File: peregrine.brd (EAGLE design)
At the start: 55.9 x 55.9 mm, 70 parts, among them IC2 LMV358IDGKR, J1 USB MICRO, U1 ITG-3200, U2 ADXL345, U4 3.3V, U5 ATMEGA32U4-XUAU, Y1 16MHz KX-7

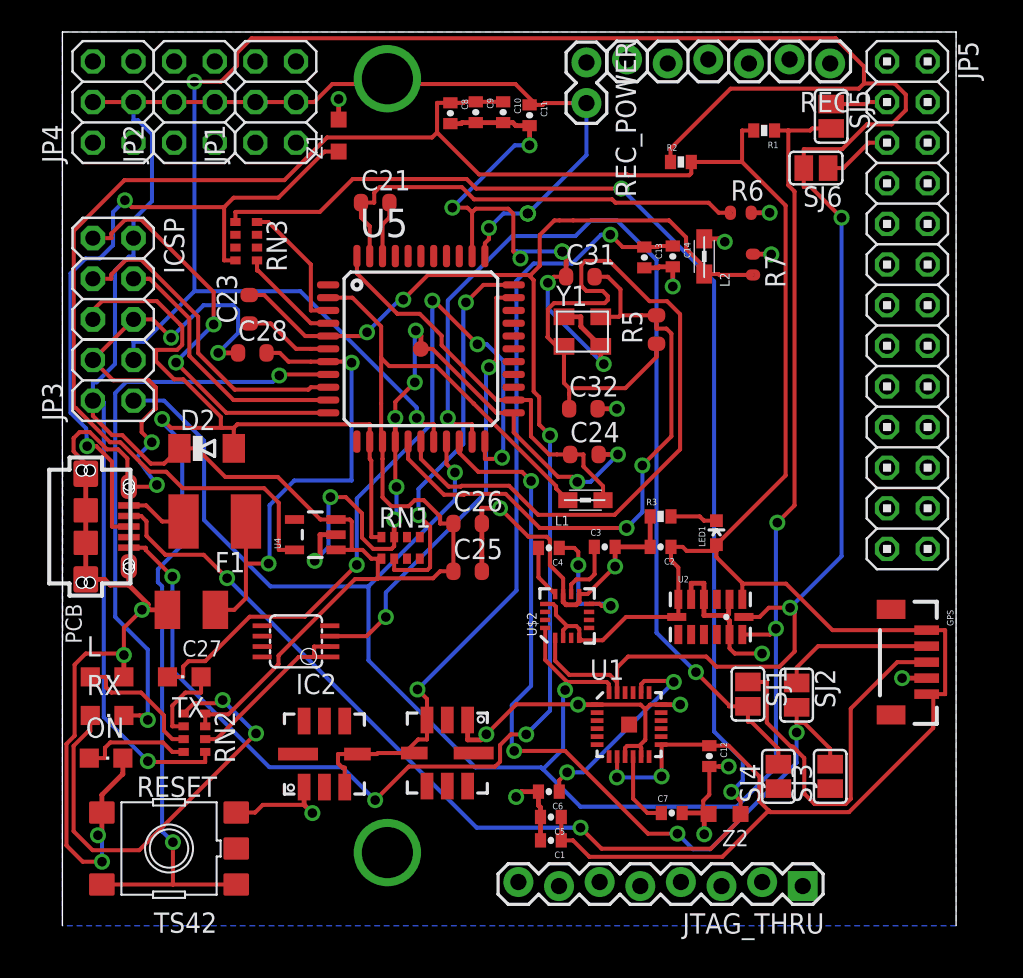
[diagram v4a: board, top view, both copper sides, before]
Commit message: Many changes.
Added level conversion to schematic. Had to re-do route because of many
added components. Also, connected a number of things which needed
connections in schematic. Route about 80% done.
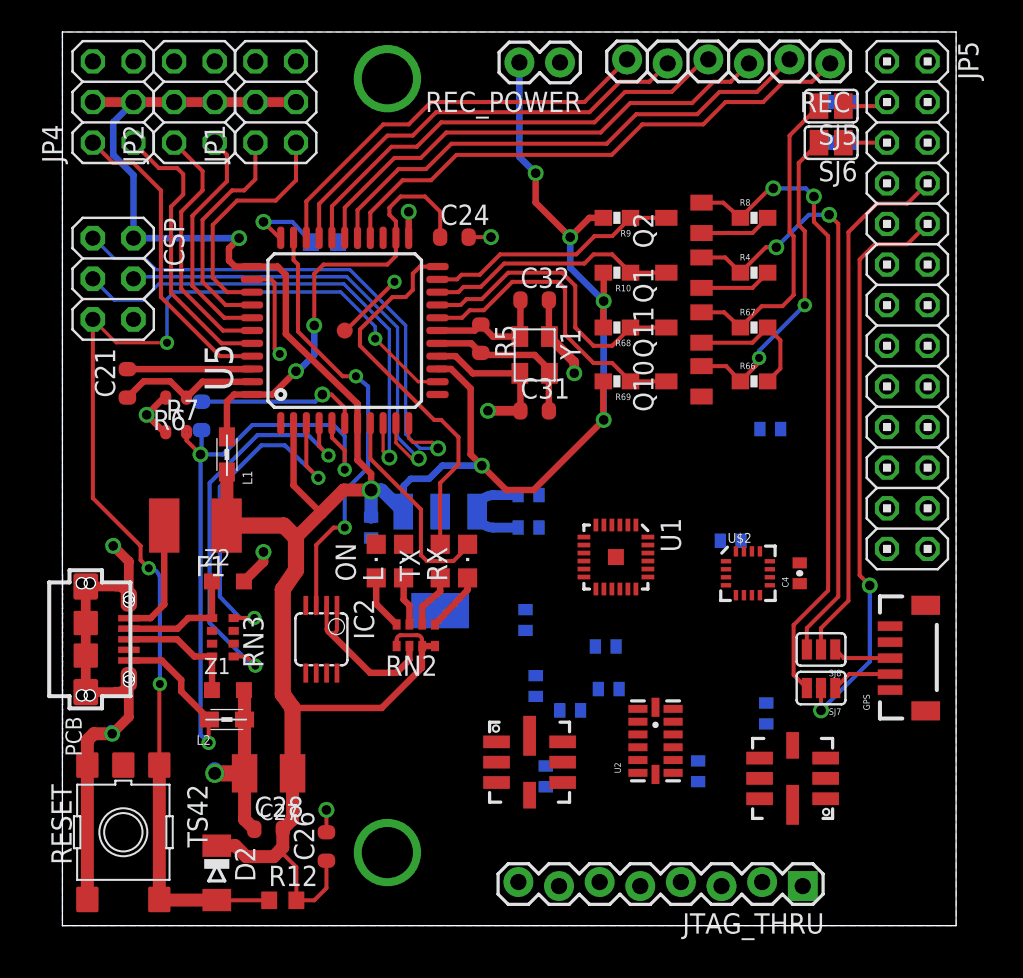
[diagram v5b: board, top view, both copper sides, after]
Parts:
- removed C25: 100n, SmartPrj:C0603-ROUND
- removed JP3: (no value), pinhead:2X02
- removed LED1: Blue, SparkFun:LED-0603
- removed R3: 330, SparkFun:0402-RES
- removed RN1: 10K, resistor-dil:CAY16
- removed SJ1, SJ2, SJ3, SJ4: (no value), jumper:SJ
- removed U4: 3.3V, SparkFun:SOT23-5
- added IC1: (no value), linear-technology:SOT223
- added Q1, Q10, Q11, Q2: BSS123, transistor-small-signal:SOT23
- added R10, R4, R66, R67, R68, R69, R8, R9: 10k, SparkFun:0603-RES
- added R11, R12: 10k, resistor:R0603
- added SJ7, SJ8: (no value), SparkFun:SJ_3
- moved L2 41.6 mm to (10.3, 12.9), turned to 0 degrees
- moved R7 37.6 mm to (7.11, 30.9), turned to 0 degrees
- moved R6 37.1 mm to (7.11, 33.0), turned to 180 degrees
- moved C8 36.2 mm to (29.6, 15.0), flipped to the bottom
- moved Z1 35.4 mm to (10.4, 14.7), turned to 0 degrees
- moved Z2 34.3 mm to (10.4, 21.5), turned to 0 degrees
- moved C14 33.5 mm to (30.2, 9.33), flipped to the bottom
- moved C13 32.3 mm to (39.8, 9.65), flipped to the bottom
- moved C9 31.9 mm to (29.0, 19.1), flipped to the bottom
- moved C28 29.8 mm to (12.9, 6.03)
- moved U$4 29.3 mm to (45.7, 9.21), turned to 180 degrees
- moved C11 27.6 mm to (19.3, 24.9), flipped to the bottom
- moved D2 26.6 mm to (9.65, 3.30), turned to 270 degrees
- moved C10 26.0 mm to (29.1, 24.9), flipped to the bottom, turned to 180 degrees
- moved RN3 24.8 mm to (10.0, 18.0)
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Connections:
- removed net 3.3V: C13.1, C14.1, U$3.3, U$3.4, U$4.3, U$4.4
- removed net A0: U5.36
- removed net A1: U5.37
- removed net A2: U5.38
- removed net A3: U5.39
- removed net A4: U5.40
- removed net A5: U5.41
- removed net D5*: U5.31
- removed net D6*: U5.27
- removed net GPS-RX: GPS.4, SJ2.1
- removed net GPS-TX: GPS.3, SJ1.1
- removed net IO10*: U5.30
- removed net IO12: U5.26
- removed net IO8: U5.28
- removed net IO9*: U5.29
- removed net M_1: JP1.2
- removed net M_2: JP2.2
- removed net M_3: JP4.2
- removed net M_4: JP1.1
- removed net M_AUX1: JP4.1
- removed net M_AUX2: JP2.1
- removed net N$10: U$3.7
- removed net N$13: U$3.6
- removed net N$15: U$4.7
- removed net N$16: U$4.6
- removed net N$4: LED1.C, R3.2
- removed net SCL: JP3.3, R2.1, SJ6.2, U$2.1, U1.23, U2.14, U5.18
- removed net SDA: JP3.1, R1.1, SJ5.2, U$2.16, U1.24, U2.13, U5.19
- removed net VUSB: C27.+, C28.2, F1.1, U5.7
- new net AT_RX3V3: Q1.2, R4.1, SJ8.3
- new net AT_TX3V3: Q2.2, R8.1, SJ7.3
- new net GPIO18(PCM_CLK): JP5.12
- new net GPS-INPUT: GPS.3, SJ8.1
- new net GPS-OUTPUT: GPS.4, SJ7.1
- new net MOT/SENS_1: JP1.1, U5.36
- new net MOT/SENS_2: JP1.2, U5.37
- new net MOT/SENS_3: JP2.1, U5.38
- new net MOT/SENS_4: JP2.2, U5.39
- new net MOT/SENS_5: JP4.1, U5.40
- new net MOT/SENS_6: JP4.2, U5.41
- new net SCL3V3: Q10.2, R2.1, R66.1, SJ6.2, U$2.1, U$3.6, U$4.6, U1.23, U2.14
- new net SCL5V: Q10.3, R69.1, U5.18
- new net SDA3V3: Q11.2, R1.1, R67.1, SJ5.2, U$2.16, U$3.7, U$4.7, U1.24, U2.13
- new net SDA5V: Q11.3, R68.1, U5.19
- net +5V: now also C27.+, C28.2, F1.1, IC1.1, R10.2, R12.2, R68.2, R69.2, R9.2, U5.7; no longer C25.1, JP3.2, RN1.5, U4.1, U4.3
- net 3V3: now also C13.1, C14.1, IC1.3, Q1.1, Q10.1, Q11.1, Q2.1, R4.2, R66.2, R67.2, R8.2, U$3.3, U$3.4, U$4.3, U$4.4; no longer LED1.A, U4.5
- net D0/RX: now also Q1.3, R10.1; no longer SJ2.2, SJ3.2
- net D1/TX: now also Q2.3, R9.1; no longer SJ1.2, SJ4.2
- net GND: now also IC1.2, IC1.4, R11.2; no longer C25.2, JP3.4, R3.1, RN1.3, U4.2
- net GPIO14(TXD): now also JP5.8, SJ8.2; no longer SJ3.1
- net GPIO15(RXD): now also JP5.10, SJ7.2; no longer SJ4.1
- net HWB: now also R11.1; no longer RN1.6
- net REC1: now also U5.26
- net REC2: now also U5.27
- net REC3: now also U5.28
- net REC4: now also U5.29
- net REC5: now also U5.30
- net REC6: now also U5.31
- net RESET: now also R12.1; no longer RN1.4
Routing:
- net GND: track 257.2 -> 80.6 mm, vias 41 -> 12
- net 3V3: track 200.1 -> 23.6 mm, vias 2 -> 0
- net SCL: track 167.7 -> 0.00 mm, vias 4 -> 0
- net SDA: track 128.4 -> 0.00 mm, vias 4 -> 0
- net D-: track 117.2 -> 7.78 mm, vias 4 -> 0
- net UGND: track 106.1 -> 45.4 mm, vias 6 -> 3
- net 3.3V: track 51.7 -> 0.00 mm, vias 2 -> 0
- net XTAL1: track 58.4 -> 7.91 mm
- net D1/TX: track 61.8 -> 15.9 mm, vias 2 -> 0
- net AT_TX3V3: track 0.00 -> 40.7 mm, vias 0 -> 2
- net AT_RX3V3: track 0.00 -> 38.1 mm, vias 0 -> 2
- net D0/RX: track 53.0 -> 15.8 mm, vias 4 -> 0
- net GPIO15(RXD): track 0.00 -> 36.3 mm, vias 0 -> 2
- net D+: track 43.8 -> 7.75 mm, vias 2 -> 0
- net REC1: track 0.00 -> 34.2 mm
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
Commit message: routing.
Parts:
- moved C3 16.3 mm to (46.9, 19.5), turned to 270 degrees
- moved C13 8.56 mm to (31.4, 11.4), turned to 90 degrees
- moved U$4 8.33 mm to (40.3, 15.6), turned to 270 degrees
- moved R2 8.15 mm to (40.8, 46.9), flipped to the top, turned to 180 degrees
- moved C8 7.31 mm to (29.8, 22.3)
- moved R1 6.93 mm to (42.1, 49.4), flipped to the top, turned to 270 degrees
- moved C14 6.81 mm to (28.1, 15.8), turned to 90 degrees
- moved C7 6.79 mm to (31.9, 21.2), flipped to the top, turned to 90 degrees
- moved C6 6.21 mm to (38.1, 22.1), flipped to the top, turned to 270 degrees
- moved U$3 5.32 mm to (28.1, 15.4)
- moved C5 4.51 mm to (40.3, 15.9)
- moved U2 4.00 mm to (34.7, 14.8)
- moved C9 3.22 mm to (28.4, 22.3)
- moved U1 2.36 mm to (35.2, 25.3)
- moved C4 1.03 mm to (46.9, 22.7)
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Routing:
- net 3V3: track 23.6 -> 193.4 mm, vias 0 -> 13
- net SDA3V3: track 19.7 -> 87.8 mm, vias 0 -> 4
- net SCL3V3: track 20.1 -> 85.3 mm, vias 2 -> 7
- net GND: track 80.6 -> 137.3 mm, vias 12 -> 22
- net N$7: track 0.00 -> 7.09 mm
- net N$2: track 0.00 -> 6.78 mm
- net N$1: track 0.00 -> 3.71 mm, vias 0 -> 1
- net N$3: track 0.00 -> 2.88 mm
- net N$5: track 0.00 -> 2.57 mm

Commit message: Fixed some stuff
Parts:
- moved C2 24.3 mm to (35.9, 8.26)
- moved C1 18.2 mm to (34.2, 8.26), flipped to the top, turned to 270 degrees
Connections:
- new net GPIO23: JP5.16
- new net GPIO24: JP5.18
- new net GPIO25: JP5.22
- new net GPIO7(CE1): JP5.26
- new net GPIO8(CE0): JP5.24
- new net PI_5V: JP5.2
- new net PI_5V_2: JP5.4
- new net PI_GND3: JP5.6
- new net PI_GND4: JP5.14
- new net PI_GND5: JP5.20
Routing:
- net GND: track 137.3 -> 139.0 mm, vias 22 -> 21
- net N$2: track 6.78 -> 6.00 mm
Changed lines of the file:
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@@
 <element name="U1" library="SparkFun" package="QFN-24" value="ITG-3200" x="35.179" y="25.3365" rot="R270"/>
 <element name="U2" library="SparkFun" package="LGA14" value="ADXL345" x="34.7345" y="14.7955" rot="R90"/>
-<element name="C1" library="SparkFun" package="0402-CAP" value="0.1uF" x="41.7195" y="24.892" rot="MR180"/>
-<element name="C2" library="SparkFun" package="0402-CAP" value="0.1uF" x="44.1325" y="31.115" rot="R270"/>
+<element name="C1" library="SparkFun" package="0402-CAP" value="0.1uF" x="34.2265" y="8.255" rot="R270"/>
+<element name="C2" library="SparkFun" package="0402-CAP" value="0.1uF" x="35.8775" y="8.255" rot="R270"/>
 <element name="C6" library="SparkFun" package="0402-CAP" value="2.2nF" x="38.1" y="22.098" rot="R270"/>
 <element name="C7" library="SparkFun" package="0402-CAP" value="0.1uF" x="31.9405" y="21.209" rot="R90"/>
@@
 <element name="JP1" library="pinhead" package="2X03" value="" x="13.335" y="51.4985" rot="R90"/>
 <element name="JP2" library="pinhead" package="2X03" value="" x="8.255" y="51.4985" rot="R90"/>
-<element name="JP4" library="pinhead" package="2X03" value="" x="3.175" y="51.4985" rot="R90"/>
+<element name="JP4" library="pinhead" package="2X03" value="" x="3.175" y="51.4985" smashed="yes" rot="R90">
+<attribute name="NAME" x="0" y="47.6885" size="1.27" layer="25" ratio="10" rot="R90"/>
+<attribute name="VALUE" x="7.62" y="47.6885" size="1.27" layer="27" rot="R90"/>
+</element>
 <element name="SJ7" library="SparkFun" package="SJ_3" value="" x="47.4345" y="14.859" rot="R180"/>
 <element name="SJ8" library="SparkFun" package="SJ_3" value="" x="47.4345" y="17.272" rot="R180"/>
@@
 <wire x1="23.8125" y1="16.0655" x2="23.8125" y2="15.9385" width="0.254" layer="16"/>
 <wire x1="23.8125" y1="15.9385" x2="23.749" y2="15.875" width="0.254" layer="16"/>
-<wire x1="44.1325" y1="30.465" x2="44.1325" y2="28.829" width="0.254" layer="1"/>
-<via x="44.1325" y="28.829" extent="1-16" drill="0.6"/>
-<wire x1="44.1325" y1="28.829" x2="44.1325" y2="28.6385" width="0.254" layer="16"/>
 <wire x1="44.2325" y1="22.2845" x2="43.1125" y2="22.2845" width="0.254" layer="1"/>
 <wire x1="43.1125" y1="22.2845" x2="42.8625" y2="22.0345" width="0.254" layer="1"/>
@@
 <wire x1="41.529" y1="17.6225" x2="41.529" y2="19.4945" width="0.254" layer="1"/>
 <wire x1="41.529" y1="19.4945" x2="41.3385" y2="19.685" width="0.254" layer="1"/>
-<via x="41.3385" y="19.685" extent="1-16" drill="0.6"/>
 <wire x1="41.3385" y1="19.685" x2="41.3385" y2="19.3525" width="0.254" layer="16"/>
 <wire x1="33.6345" y1="13.5955" x2="33.6345" y2="14.3955" width="0.254" layer="1"/>
@@
 <via x="44.8945" y="20.5105" extent="1-16" drill="0.6"/>
 <wire x1="44.8945" y1="20.5105" x2="44.8945" y2="20.32" width="0.254" layer="16"/>
+<wire x1="34.2265" y1="7.605" x2="35.8775" y2="7.605" width="0.254" layer="1"/>
+<wire x1="34.2265" y1="7.605" x2="32.878" y2="7.605" width="0.254" layer="1"/>
+<wire x1="32.878" y1="7.605" x2="32.5755" y2="7.3025" width="0.254" layer="1"/>
+<via x="32.5755" y="7.3025" extent="1-16" drill="0.6"/>
+<wire x1="32.5755" y1="7.3025" x2="32.5755" y2="7.239" width="0.254" layer="16"/>
+<wire x1="32.5755" y1="7.239" x2="32.512" y2="7.1755" width="0.254" layer="16"/>
 </signal>
 <signal name="N$5">
@@
 <contactref element="C4" pad="1"/>
 <wire x1="46.863" y1="22.083" x2="46.863" y2="20.955" width="0.254" layer="1"/>
-<wire x1="43.6125" y1="20.6645" x2="43.6125" y2="19.3795" width="0.254" layer="1"/>
-<wire x1="43.6125" y1="19.3795" x2="43.942" y2="19.05" width="0.254" layer="1"/>
-<wire x1="43.942" y1="19.05" x2="45.2755" y2="19.05" width="0.254" layer="1"/>
-<wire x1="45.2755" y1="19.05" x2="45.6565" y2="19.431" width="0.254" layer="1"/>
-<wire x1="45.6565" y1="19.431" x2="45.6565" y2="19.7485" width="0.254" layer="1"/>
-<wire x1="45.6565" y1="19.7485" x2="46.863" y2="20.955" width="0.254" layer="1"/>
+<wire x1="43.6125" y1="20.6645" x2="43.6125" y2="19.7605" width="0.254" layer="1"/>
+<wire x1="43.6125" y1="19.7605" x2="43.8785" y2="19.4945" width="0.254" layer="1"/>
+<wire x1="43.8785" y1="19.4945" x2="45.4025" y2="19.4945" width="0.254" layer="1"/>
+<wire x1="45.4025" y1="19.4945" x2="46.863" y2="20.955" width="0.254" layer="1"/>
 </signal>
 <signal name="N$3">
@@
 <wire x1="31.4325" y1="27.432" x2="31.4325" y2="26.15" width="0.254" layer="1"/>
 <wire x1="31.4325" y1="26.15" x2="31.369" y2="26.0865" width="0.254" layer="1"/>
-<wire x1="44.0935" y1="34.036" x2="44.0935" y2="31.804" width="0.254" layer="1"/>
-<wire x1="44.0935" y1="31.804" x2="44.1325" y2="31.765" width="0.254" layer="1"/>
 <wire x1="51.7525" y1="18.732" x2="53.0865" y2="18.732" width="0.254" layer="1"/>
 <wire x1="53.0865" y1="18.732" x2="53.4035" y2="18.415" width="0.254" layer="1"/>
@@
 <wire x1="41.4965" y1="22.2885" x2="41.4925" y2="22.2845" width="0.254" layer="1"/>
 <wire x1="41.4965" y1="22.2885" x2="40.894" y2="22.2885" width="0.254" layer="1"/>
-<wire x1="40.894" y1="22.2885" x2="40.767" y2="22.1615" width="0.254" layer="1"/>
-<wire x1="40.767" y1="22.1615" x2="40.767" y2="21.7805" width="0.254" layer="1"/>
+<wire x1="40.894" y1="22.2885" x2="40.8305" y2="22.225" width="0.254" layer="1"/>
+<wire x1="40.8305" y1="22.225" x2="40.767" y2="22.1615" width="0.254" layer="1"/>
+<wire x1="40.767" y1="22.1615" x2="40.767" y2="21.9075" width="0.254" layer="1"/>
+<wire x1="40.767" y1="21.9075" x2="40.767" y2="21.7805" width="0.254" layer="1"/>
 <wire x1="40.767" y1="21.7805" x2="40.767" y2="21.463" width="0.254" layer="1"/>
 <wire x1="40.767" y1="21.463" x2="40.894" y2="21.336" width="0.254" layer="1"/>
@@
 <wire x1="37.465" y1="10.4775" x2="34.3535" y2="10.4775" width="0.254" layer="1"/>
 <wire x1="34.3535" y1="10.4775" x2="34.0995" y2="10.7315" width="0.254" layer="1"/>
-<wire x1="41.0695" y1="24.892" x2="39.878" y2="24.892" width="0.254" layer="16"/>
-<wire x1="39.878" y1="24.892" x2="39.116" y2="24.13" width="0.254" layer="16"/>
-<wire x1="39.116" y1="24.13" x2="39.116" y2="22.2885" width="0.254" layer="16"/>
-<wire x1="39.116" y1="22.2885" x2="39.497" y2="21.9075" width="0.254" layer="16"/>
-<via x="39.497" y="21.9075" extent="1-16" drill="0.6"/>
 <wire x1="39.497" y1="21.9075" x2="40.64" y2="21.9075" width="0.254" layer="1"/>
 <wire x1="40.64" y1="21.9075" x2="40.767" y2="21.7805" width="0.254" layer="1"/>
@@
 <wire x1="43.6125" y1="24.0545" x2="44.1325" y2="24.5745" width="0.254" layer="1"/>
 <via x="44.1325" y="24.5745" extent="1-16" drill="0.6"/>
-<wire x1="44.1325" y1="24.5745" x2="44.1325" y2="23.4315" width="0.254" layer="16"/>
-<wire x1="44.1325" y1="23.4315" x2="43.6245" y2="22.9235" width="0.254" layer="16"/>
-<wire x1="43.6245" y1="22.9235" x2="41.91" y2="22.9235" width="0.254" layer="16"/>
-<wire x1="41.91" y1="22.9235" x2="41.0845" y2="23.749" width="0.254" layer="16"/>
-<wire x1="41.0845" y1="23.749" x2="41.0845" y2="24.877" width="0.254" layer="16"/>
-<wire x1="41.0845" y1="24.877" x2="41.0695" y2="24.892" width="0.254" layer="16"/>
 <wire x1="39.497" y1="21.9075" x2="39.497" y2="19.939" width="0.254" layer="16"/>
 <wire x1="39.497" y1="19.939" x2="38.989" y2="19.431" width="0.254" layer="16"/>
@@
 <wire x1="46.609" y1="23.241" x2="45.2755" y2="24.5745" width="0.254" layer="16"/>
 <wire x1="45.2755" y1="24.5745" x2="44.1325" y2="24.5745" width="0.254" layer="16"/>
+<wire x1="41.4925" y1="22.2845" x2="40.89" y2="22.2845" width="0.254" layer="1"/>
+<wire x1="40.89" y1="22.2845" x2="40.8305" y2="22.225" width="0.254" layer="1"/>
+<wire x1="40.8305" y1="22.225" x2="40.767" y2="22.1615" width="0.254" layer="1"/>
+<wire x1="40.767" y1="22.1615" x2="40.767" y2="21.9075" width="0.254" layer="1"/>
+<wire x1="40.767" y1="21.9075" x2="39.497" y2="21.9075" width="0.254" layer="1"/>
+<wire x1="39.497" y1="21.9075" x2="39.497" y2="24.003" width="0.254" layer="16"/>
+<wire x1="39.497" y1="24.003" x2="40.1955" y2="24.7015" width="0.254" layer="16"/>
+<wire x1="40.1955" y1="24.7015" x2="44.0055" y2="24.7015" width="0.254" layer="16"/>
+<wire x1="44.0055" y1="24.7015" x2="44.1325" y2="24.5745" width="0.254" layer="16"/>
+<wire x1="34.2265" y1="8.905" x2="34.2265" y2="10.6045" width="0.254" layer="1"/>
+<wire x1="34.2265" y1="10.6045" x2="34.0995" y2="10.7315" width="0.254" layer="1"/>
+<wire x1="35.8775" y1="8.905" x2="34.2265" y2="8.905" width="0.254" layer="1"/>
+<via x="39.497" y="21.9075" extent="1-16" drill="0.6"/>
 </signal>
 <signal name="REC1">
@@
 <contactref element="JP5" pad="12"/>
 </signal>
+<signal name="PI_5V">
+<contactref element="JP5" pad="2"/>
+</signal>
+<signal name="PI_5V_2">
+<contactref element="JP5" pad="4"/>
+</signal>
+<signal name="PI_GND3">
+<contactref element="JP5" pad="6"/>
+</signal>
+<signal name="PI_GND4">
+<contactref element="JP5" pad="14"/>
+</signal>
+<signal name="GPIO23">
+<contactref element="JP5" pad="16"/>
+</signal>
+<signal name="GPIO24">
+<contactref element="JP5" pad="18"/>
+</signal>
+<signal name="PI_GND5">
+<contactref element="JP5" pad="20"/>
+</signal>
+<signal name="GPIO25">
+<contactref element="JP5" pad="22"/>
+</signal>
+<signal name="GPIO8(CE0)">
+<contactref element="JP5" pad="24"/>
+</signal>
+<signal name="GPIO7(CE1)">
+<contactref element="JP5" pad="26"/>
+</signal>
 </signals>
